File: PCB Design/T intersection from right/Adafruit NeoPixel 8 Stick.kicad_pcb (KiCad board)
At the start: 2 copper layers, 36.2 x 28.6 mm, 8 parts, among them CN1 1X4SMT, CN2 1X4SMT, CN3 1X4SMT

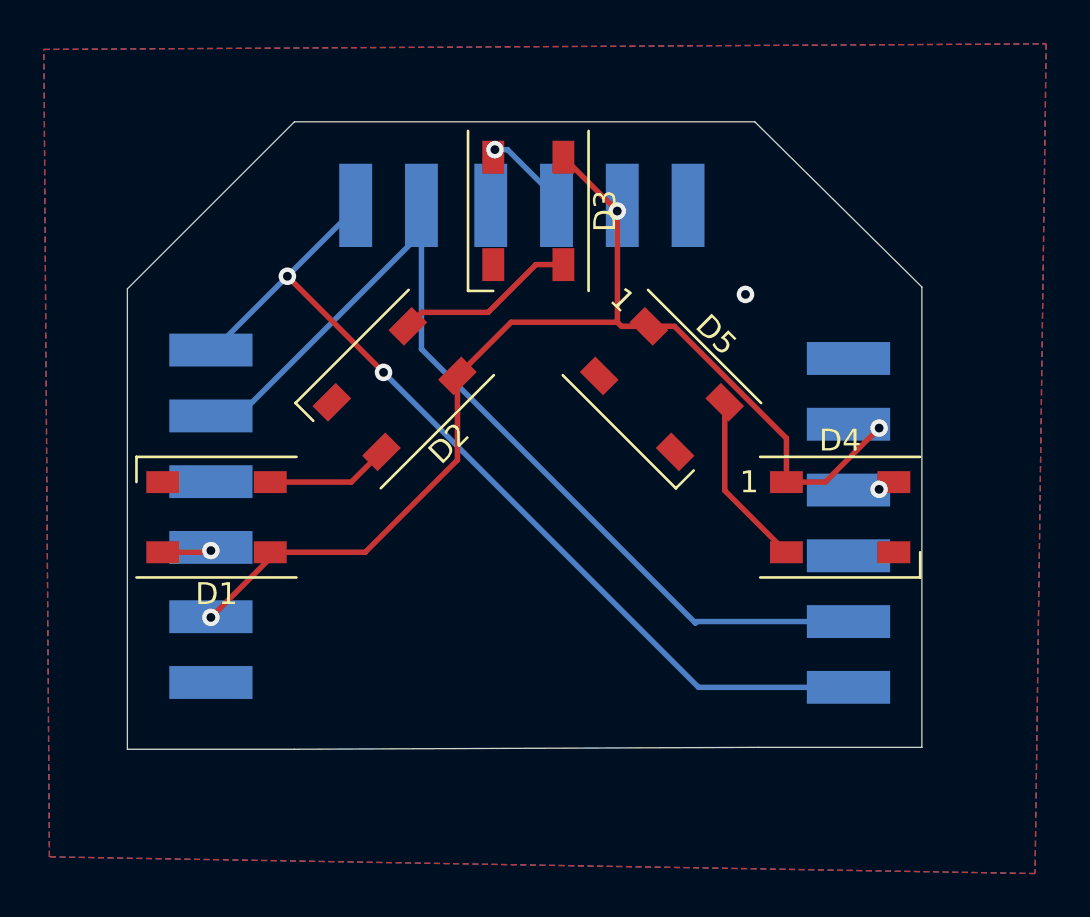
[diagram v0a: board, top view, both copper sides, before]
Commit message: move vias off pads
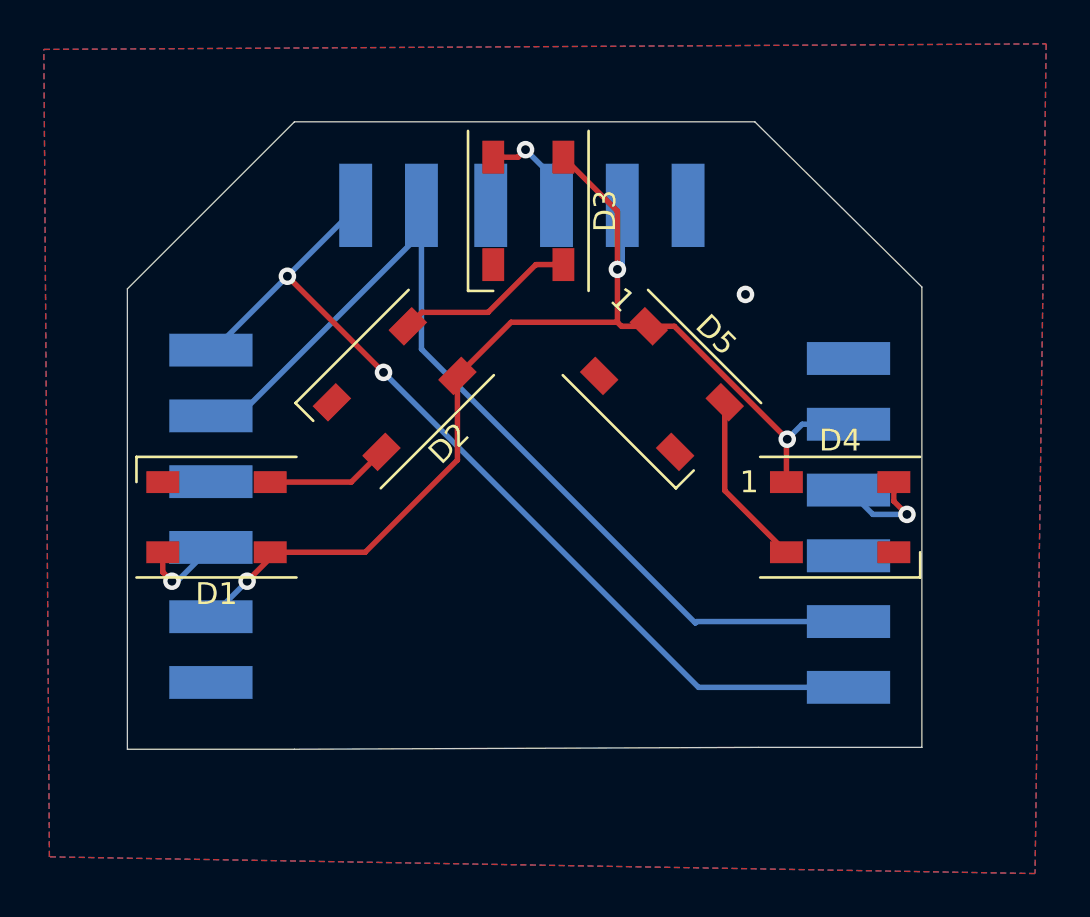
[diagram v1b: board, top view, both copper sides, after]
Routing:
- net Net-(CN3-Pad3): track 0.00 -> 4.85 mm
- net Net-(CN2-Pad3): track 2.23 -> 3.91 mm
- net +5V: track 52.0 -> 53.0 mm
- net Net-(CN1-Pad4): track 4.04 -> 4.74 mm
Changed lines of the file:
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@@
   (segment (start 137.483782 101.506959) (end 139.930741 99.06) (width 0.25) (layer "F.Cu") (net 1))
   (segment (start 152.49 104.352007) (end 152.49 106.35) (width 0.25) (layer "F.Cu") (net 1))
+  (segment (start 128.942 109.818) (end 127.889 110.871) (width 0.25) (layer "F.Cu") (net 1))
   (segment (start 139.930741 99.06) (end 144.78 99.06) (width 0.25) (layer "F.Cu") (net 1))
   (segment (start 144.773 93.987) (end 142.316 91.53) (width 0.25) (layer "F.Cu") (net 1))
@@
   (segment (start 128.942 109.55) (end 133.274 109.55) (width 0.25) (layer "F.Cu") (net 1))
   (segment (start 137.483782 105.340218) (end 137.483782 101.506959) (width 0.25) (layer "F.Cu") (net 1))
-  (segment (start 126.238 112.522) (end 128.942 109.818) (width 0.25) (layer "F.Cu") (net 1))
   (segment (start 146.210959 99.244218) (end 144.964218 99.244218) (width 0.25) (layer "F.Cu") (net 1))
-  (segment (start 152.49 106.35) (end 154.254 106.35) (width 0.25) (layer "F.Cu") (net 1))
-  (segment (start 154.254 106.35) (end 156.718 103.886) (width 0.25) (layer "F.Cu") (net 1))
+  (segment (start 128.942 109.55) (end 128.942 109.818) (width 0.25) (layer "F.Cu") (net 1))
   (segment (start 144.964218 99.244218) (end 144.78 99.06) (width 0.25) (layer "F.Cu") (net 1))
   (segment (start 147.382211 99.244218) (end 152.49 104.352007) (width 0.25) (layer "F.Cu") (net 1))
-  (via (at 126.238 112.522) (size 0.8) (drill 0.4) (layers "F.Cu" "B.Cu") (net 1))
-  (via (at 144.773 93.987) (size 0.8) (drill 0.4) (layers "F.Cu" "B.Cu") (net 1))
-  (via (at 156.718 103.886) (size 0.8) (drill 0.4) (layers "F.Cu" "B.Cu") (net 1))
+  (via (at 127.889 110.871) (size 0.8) (drill 0.4) (layers "F.Cu" "B.Cu") (net 1))
+  (via (at 144.78 96.647) (size 0.8) (drill 0.4) (layers "F.Cu" "B.Cu") (net 1))
+  (via (at 152.527 104.394) (size 0.8) (drill 0.4) (layers "F.Cu" "B.Cu") (net 1))
+  (segment (start 145.002 96.425) (end 144.78 96.647) (width 0.25) (layer "B.Cu") (net 1))
+  (segment (start 126.238 112.49) (end 126.27 112.49) (width 0.25) (layer "B.Cu") (net 1))
+  (segment (start 153.209 103.712) (end 152.527 104.394) (width 0.25) (layer "B.Cu") (net 1))
+  (segment (start 155.321 103.712) (end 153.209 103.712) (width 0.25) (layer "B.Cu") (net 1))
+  (segment (start 145.002 93.726) (end 145.002 96.425) (width 0.25) (layer "B.Cu") (net 1))
+  (segment (start 126.27 112.49) (end 127.889 110.871) (width 0.25) (layer "B.Cu") (net 1))
   (via (at 150.622 97.79) (size 0.8) (drill 0.4) (layers "F.Cu" "B.Cu") (free) (net 2))
   (segment (start 135.842 93.726) (end 135.842 100.282) (width 0.25) (layer "B.Cu") (net 3))
@@
   (segment (start 148.336 112.776) (end 148.4 112.712) (width 0.25) (layer "B.Cu") (net 3))
   (segment (start 148.4 112.712) (end 155.321 112.712) (width 0.25) (layer "B.Cu") (net 3))
-  (segment (start 126.162 109.55) (end 126.238 109.474) (width 0.25) (layer "F.Cu") (net 4))
-  (segment (start 124.042 109.55) (end 126.162 109.55) (width 0.25) (layer "F.Cu") (net 4))
-  (via (at 126.238 109.474) (size 0.8) (drill 0.4) (layers "F.Cu" "B.Cu") (net 4))
+  (segment (start 124.042 110.453) (end 124.46 110.871) (width 0.25) (layer "F.Cu") (net 4))
+  (segment (start 124.042 109.55) (end 124.042 110.453) (width 0.25) (layer "F.Cu") (net 4))
+  (via (at 124.46 110.871) (size 0.8) (drill 0.4) (layers "F.Cu" "B.Cu") (net 4))
+  (segment (start 124.46 110.871) (end 124.697 110.871) (width 0.25) (layer "B.Cu") (net 4))
+  (segment (start 124.697 110.871) (end 126.238 109.33) (width 0.25) (layer "B.Cu") (net 4))
   (segment (start 128.942 106.35) (end 132.640741 106.35) (width 0.25) (layer "F.Cu") (net 5))
   (segment (start 132.640741 106.35) (end 134.018959 104.971782) (width 0.25) (layer "F.Cu") (net 5))
@@
   (segment (start 134.112 101.346) (end 148.478 115.712) (width 0.25) (layer "B.Cu") (net 7))
   (segment (start 148.478 115.712) (end 155.321 115.712) (width 0.25) (layer "B.Cu") (net 7))
-  (via (at 139.192 91.186) (size 0.8) (drill 0.4) (layers "F.Cu" "B.Cu") (net 8))
-  (segment (start 139.7684 91.186) (end 142.002 93.4196) (width 0.25) (layer "B.Cu") (net 8))
-  (segment (start 142.002 93.4196) (end 142.002 93.726) (width 0.25) (layer "B.Cu") (net 8))
-  (segment (start 139.192 91.186) (end 139.7684 91.186) (width 0.25) (layer "B.Cu") (net 8))
-  (via (at 156.718 106.68) (size 0.8) (drill 0.4) (layers "F.Cu" "B.Cu") (net 9))
+  (segment (start 140.245 91.53) (end 140.589 91.186) (width 0.25) (layer "F.Cu") (net 8))
+  (segment (start 139.116 91.53) (end 140.245 91.53) (width 0.25) (layer "F.Cu") (net 8))
+  (via (at 140.589 91.186) (size 0.8) (drill 0.4) (layers "F.Cu" "B.Cu") (net 8))
+  (segment (start 142.002 92.599) (end 142.002 93.726) (width 0.25) (layer "B.Cu") (net 8))
+  (segment (start 140.589 91.186) (end 142.002 92.599) (width 0.25) (layer "B.Cu") (net 8))
+  (segment (start 157.39 107.225) (end 157.988 107.823) (width 0.25) (layer "F.Cu") (net 9))
+  (segment (start 157.39 106.35) (end 157.39 107.225) (width 0.25) (layer "F.Cu") (net 9))
+  (via (at 157.988 107.823) (size 0.8) (drill 0.4) (layers "F.Cu" "B.Cu") (net 9))
+  (segment (start 156.432 107.823) (end 157.988 107.823) (width 0.25) (layer "B.Cu") (net 9))
+  (segment (start 155.321 106.712) (end 156.432 107.823) (width 0.25) (layer "B.Cu") (net 9))
   (segment (start 149.675782 102.709041) (end 149.675782 106.735782) (width 0.25) (layer "F.Cu") (net 11))
   (segment (start 149.675782 106.735782) (end 152.49 109.55) (width 0.25) (layer "F.Cu") (net 11))
